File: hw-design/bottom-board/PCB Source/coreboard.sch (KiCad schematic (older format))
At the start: 21 parts, among them J5 HMI_DATA, J6 SERIAL_DEBUG, U3 AP2120N-3.3, U7 AT24CS08

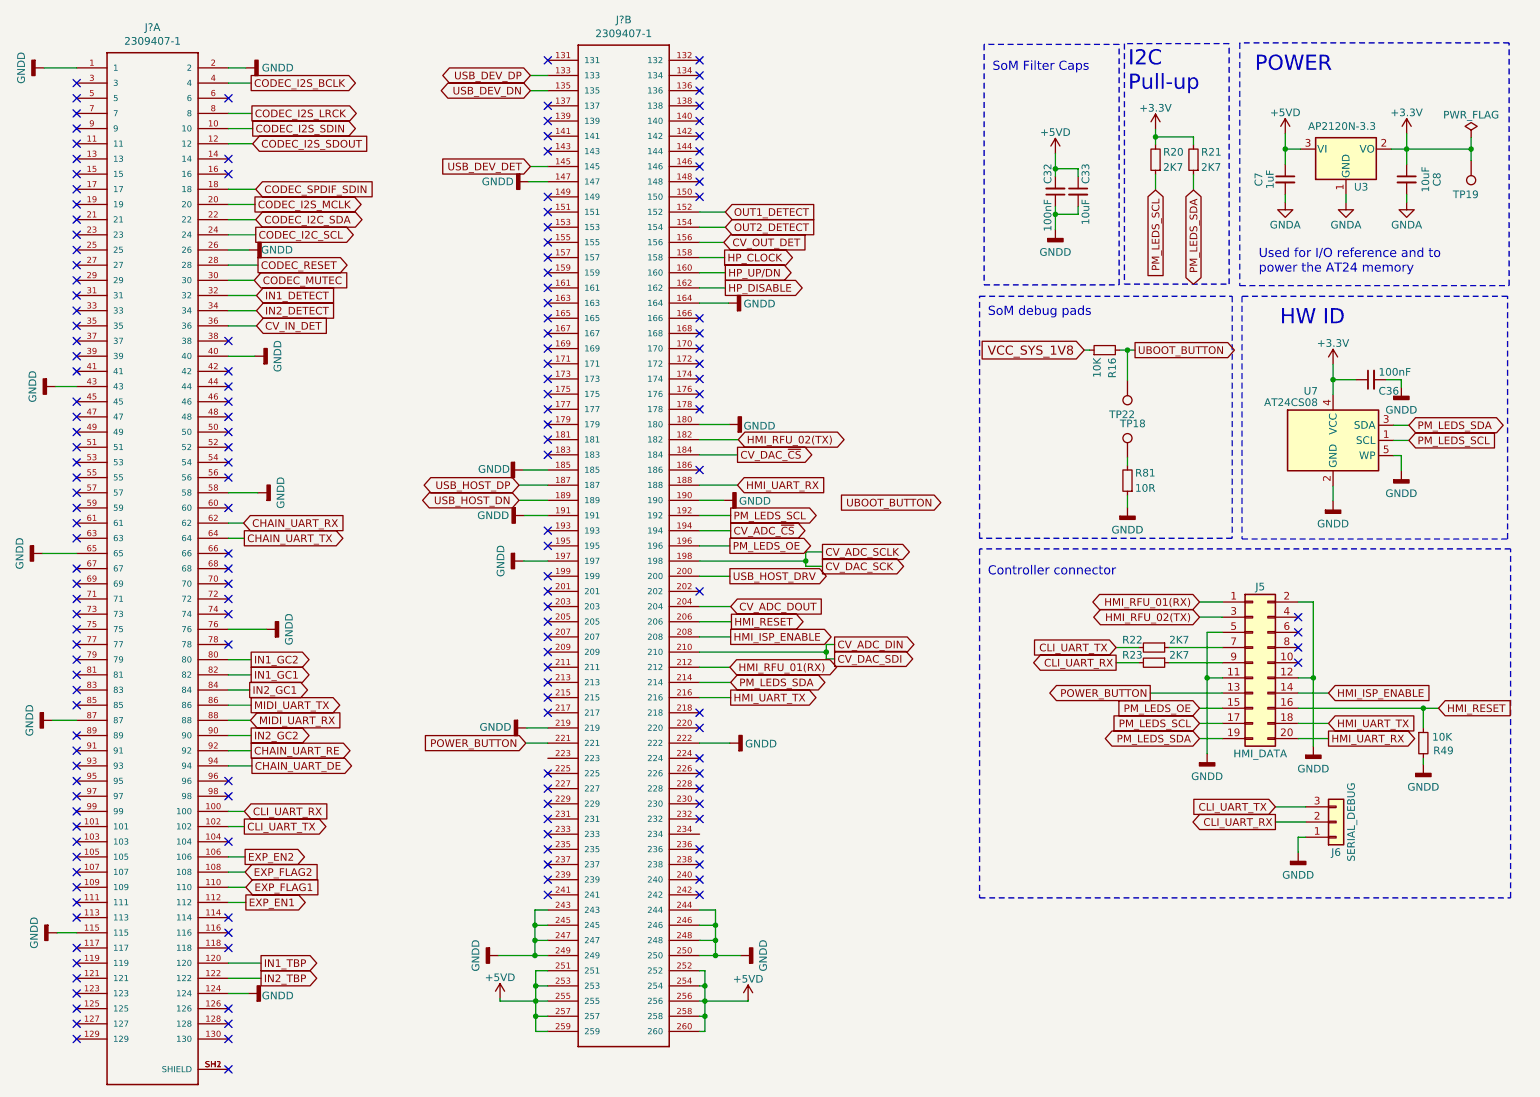
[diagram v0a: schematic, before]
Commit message: place new power curcuit on the PCB
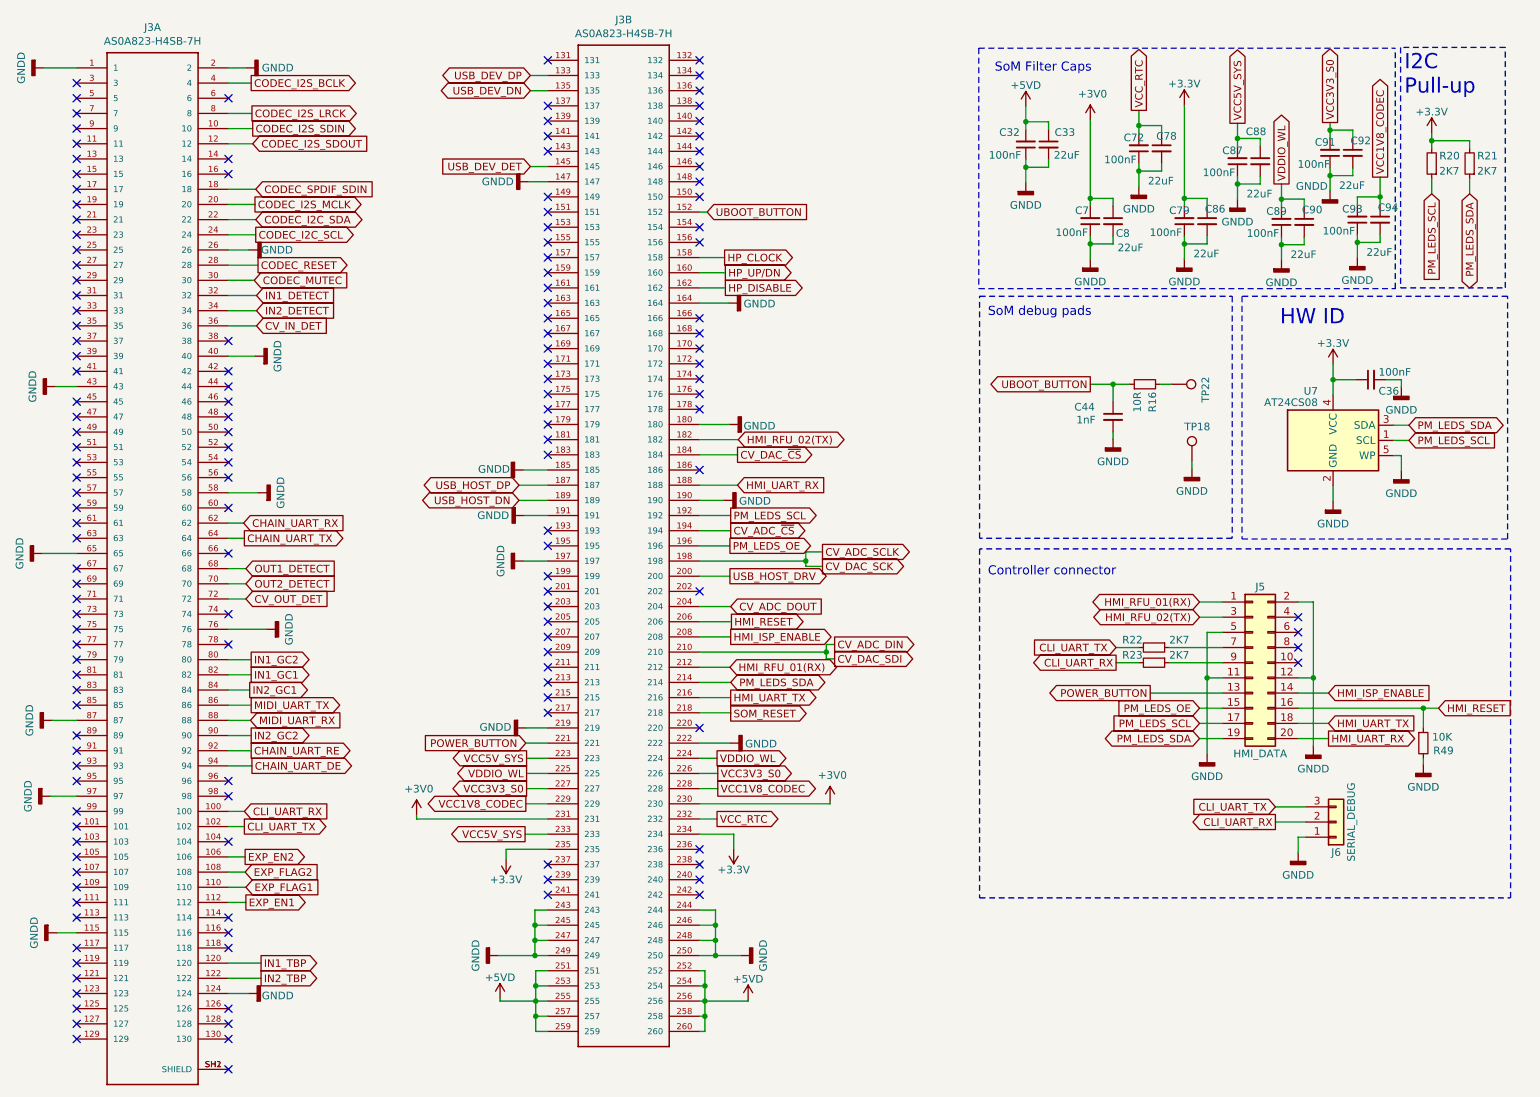
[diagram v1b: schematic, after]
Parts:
- removed R81: 10R, Resistor_SMD:R_0603_1608Metric, symbol bottom-board-rescue:R_Small-Device
- removed TP19: TestPoint, TestPoint:TestPoint_Pad_D1.0mm, symbol bottom-board-rescue:TestPoint-Connector
- removed U3: AP2120N-3.3, Package_TO_SOT_SMD:SOT-23, symbol bottom-board-rescue:AP2120N-3.3-local-components
- added C44: 1nF, Capacitor_SMD:C_0603_1608Metric, symbol bottom-board-rescue:C_Small-Device
- added C72, C79, C87, C89, C91, C93: 100nF, Capacitor_SMD:C_0603_1608Metric, symbol bottom-board-rescue:C_Small-Device
- added C78, C86, C88, C90, C92, C94: 22uF, Capacitor_SMD:C_0805_2012Metric, symbol bottom-board-rescue:C_Small-Device
- C33, C8: value 10uF -> 22uF; footprint Capacitor_SMD:C_0603_1608Metric -> Capacitor_SMD:C_0805_2012Metric; MPN CL10A106MQ8NNNC -> CL21A226MPQNNNE
- C7: value 1uF -> 100nF; MPN CL10B105KP8NNNC -> GCM188R71C104KA37D
- J3: renamed from J?; value 2309407-1 -> AS0A823-H4SB-7H; footprint TE_2309407-1 -> Uno:TE_2309409-1; Field10 TE Connectivity -> (none); Field11 DDR4 SODIMM Socket 260 Contacts 0.5mm Pitch Black Surface M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 -> (none); Field12 260 -> (none); Field13 .5 mm[.0197 in] -> (none); Field14 Socket -> (none); Field4 None -> (none); Field5 2309407-1 -> (none); Field6 None -> (none); Field7 https://www.te.com/usa-en/product-2309407-1.html?te_bu=Cor&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 -> (none); Field8 Unavailable -> (none); Field9 Compliant -> (none); MPN (none) -> AS0A823-H4SB-7H
- R16: value 10K -> 10R; MPN RR0816P-103-D -> (none)
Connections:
- net VCC_SYS_1V8 is gone; now on net UBOOT_BUTTON: R16.1
- net +3V3: now also J3.234, J3.235, C79.2, C86.1; no longer C8.1
- net +5VD: no longer C7.1
- net CV_OUT_DET: now also J3.72; no longer J3.156
- net GNDD: now also C7.1, C8.2, J3.97, TP18.1, C44.2, C72.1, C78.2, C79.1, C86.2, C87.1, C88.2, C89.1, C90.2, C91.1, C92.2, C93.1, C94.2
- net OUT1_DETECT: now also J3.68; no longer J3.152
- net OUT2_DETECT: now also J3.70; no longer J3.154
- net UBOOT_BUTTON: now also J3.152, C44.1; no longer R16.2, TP22.1
- net SOM_RESET: now reaches J3.218
- net VCC5V_SYS: now reaches J3.223
- net VCC5V_SYS: now also J3.233, C87.2, C88.1
- net VDDIO_WL: now reaches J3.224
- net VDDIO_WL: now also J3.225, C89.2, C90.1
- net VCC3V3_S0: now reaches J3.226
- net VCC3V3_S0: now also J3.227, C91.2, C92.1
- net VCC1V8_CODEC: now reaches J3.228
- net VCC1V8_CODEC: now also J3.229, C93.2, C94.1
- net +3V0: now reaches J3.230
- net +3V0: now also C7.2, C8.1, J3.231
- net VCC_RTC: now reaches J3.232
- net VCC_RTC: now also C72.2, C78.1
- removed net GNDA: C7.2, C8.2
- new net: R16.2, TP22.1
- no-connect marks 167 -> 153
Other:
- note removed: "POWER"
- note removed: "Used for I/O reference and to\npower the AT24 memory"
- moved on the sheet: C32, C33, R16, R20, R21, TP18, TP22

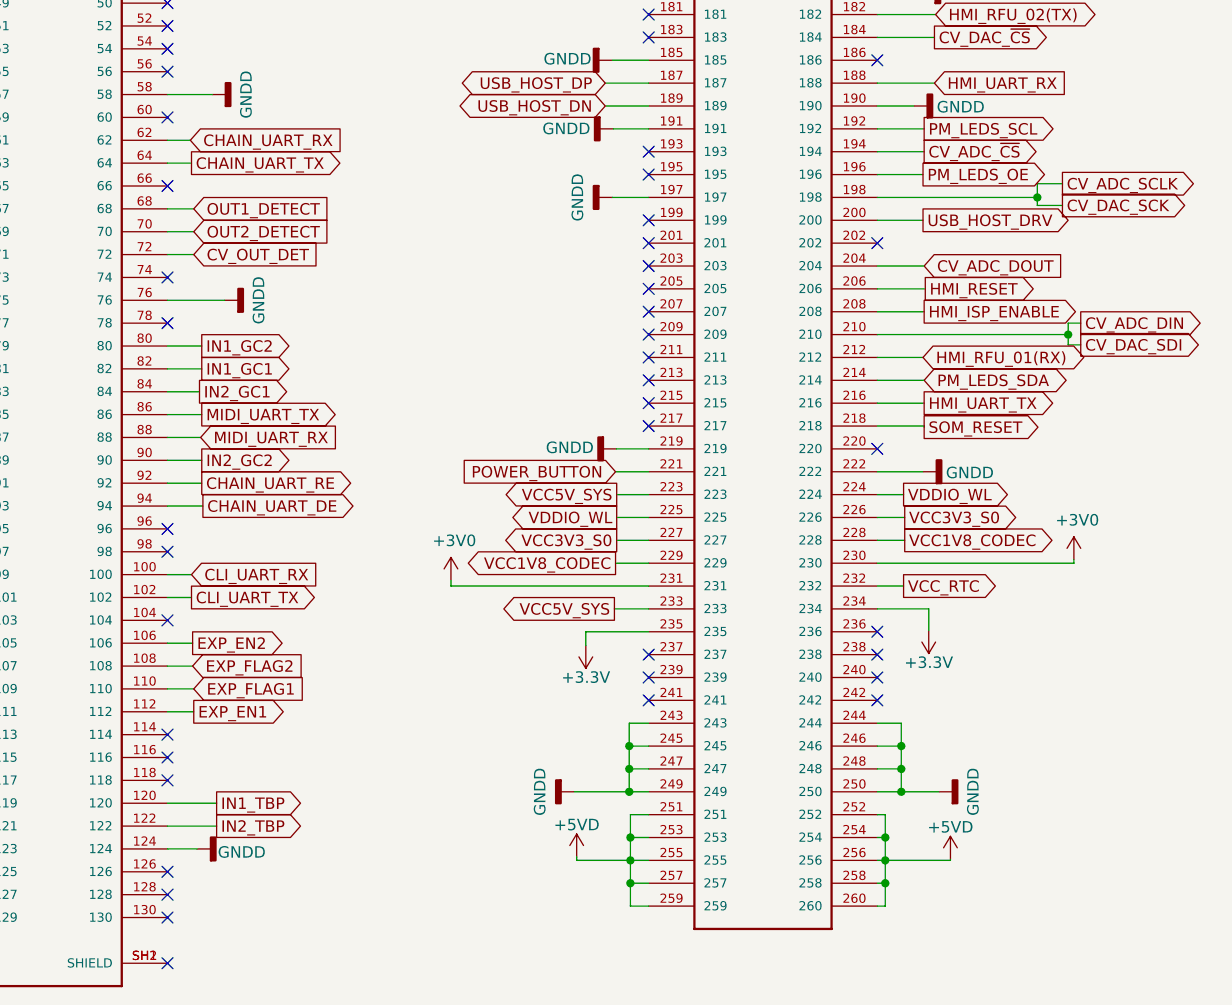
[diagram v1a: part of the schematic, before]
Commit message: route codec to new SoM
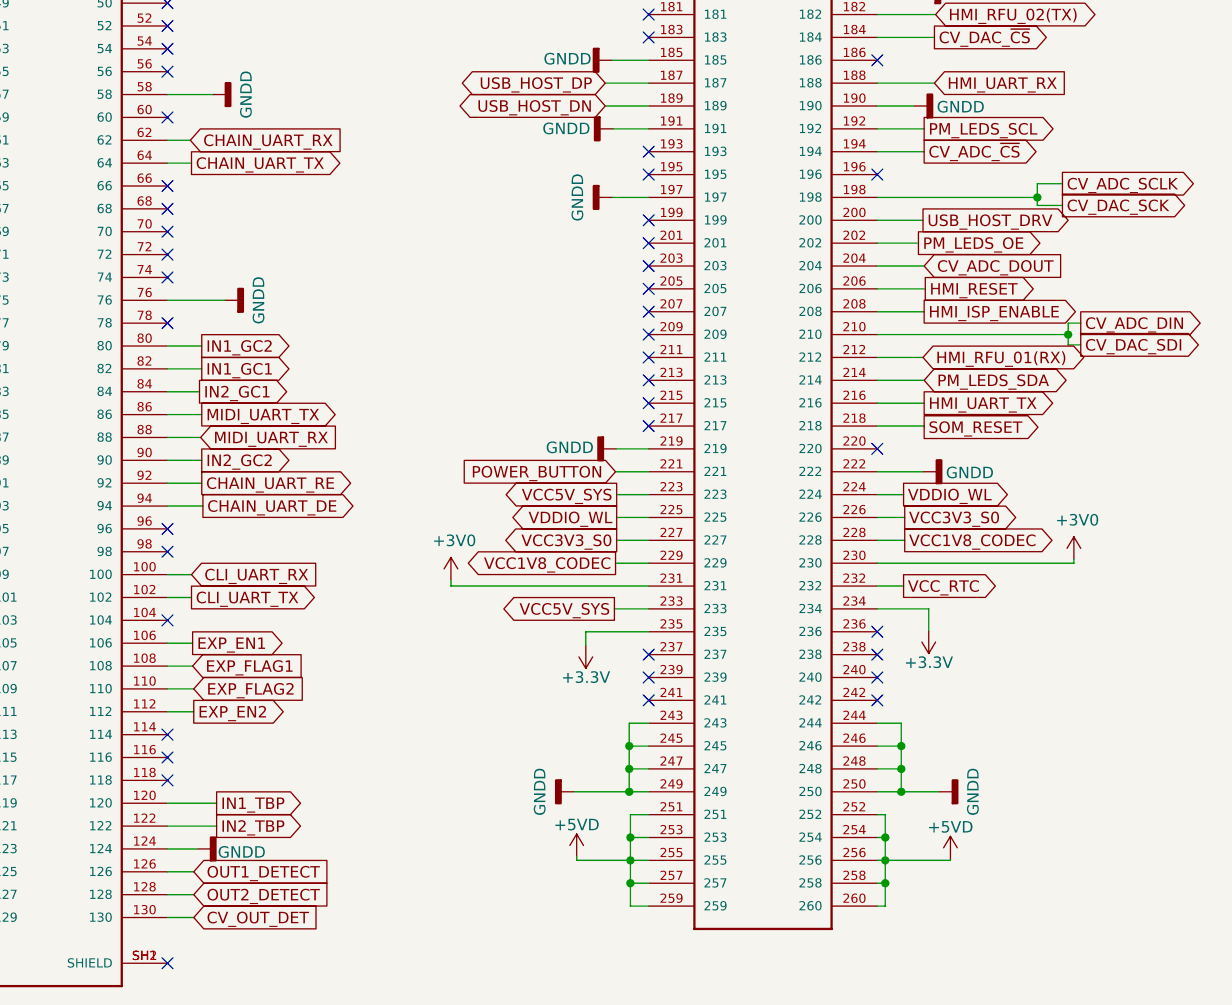
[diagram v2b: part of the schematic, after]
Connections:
- net CV_OUT_DET: now also J3.130; no longer J3.72
- net EXP_EN1: now also J3.106; no longer J3.112
- net EXP_EN2: now also J3.112; no longer J3.106
- net EXP_FLAG1: now also J3.108; no longer J3.110
- net EXP_FLAG2: now also J3.110; no longer J3.108
- net OUT1_DETECT: now also J3.126; no longer J3.68
- net OUT2_DETECT: now also J3.128; no longer J3.70
- net PM_LEDS_OE: now also J3.202; no longer J3.196
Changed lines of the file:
@@
 Text GLabel 2835 2690 2    50   Input ~ 0
 CV_IN_DET
-Text GLabel 2765 4490 2    50   Input ~ 0
+Text GLabel 2765 7390 2    50   Input ~ 0
 CV_OUT_DET
 Text GLabel 4640 1040 0    50   BiDi ~ 0
@@
 Text GLabel 5960 3940 2    50   Output ~ 0
 PM_LEDS_SCL
-Text GLabel 5955 4140 2    50   Output ~ 0
+Text GLabel 5935 4440 2    50   Output ~ 0
 PM_LEDS_OE
 Text GLabel 6005 3740 2    50   Input ~ 0
@@
 Text GLabel 5965 4640 2    50   Output ~ 0
 HMI_RESET
+Text GLabel 2765 6390 2    50   Input ~ 0
+EXP_FLAG2
 Text GLabel 2760 6290 2    50   Input ~ 0
-EXP_FLAG2
-Text GLabel 2765 6390 2    50   Input ~ 0
 EXP_FLAG1
+Text GLabel 2760 6190 2    50   Output ~ 0
+EXP_EN1
 Text GLabel 2765 6490 2    50   Output ~ 0
-EXP_EN1
-Text GLabel 2760 6190 2    50   Output ~ 0
 EXP_EN2
 Text GLabel 2845 2290 2    50   Output ~ 0
@@
 Text GLabel 2835 2590 2    50   Input ~ 0
 IN2_DETECT
-Text GLabel 2765 4290 2    50   Input ~ 0
+Text GLabel 2765 7190 2    50   Input ~ 0
 OUT1_DETECT
-Text GLabel 2765 4390 2    50   Input ~ 0
+Text GLabel 2765 7290 2    50   Input ~ 0
 OUT2_DETECT
 $Comp
@@
 Wire Wire Line
 	5755 4040 5960 4040
-Wire Wire Line
-	5755 4140 5955 4140
 Wire Wire Line
 	5755 4340 5955 4340
@@
 NoConn ~ 1650 7290
 NoConn ~ 1650 7390
-NoConn ~ 2650 7390
-NoConn ~ 2650 7290
-NoConn ~ 2650 7190
 NoConn ~ 2650 6790
 NoConn ~ 2650 6690
@@
 NoConn ~ 4755 5240
 NoConn ~ 5755 5340
-NoConn ~ 5755 4440
 NoConn ~ 5755 3640
 NoConn ~ 5755 3240
@@
 	1650 5790 1480 5790
 Wire Wire Line
-	2650 4290 2765 4290
-Wire Wire Line
-	2650 4390 2765 4390
-Wire Wire Line
-	2650 4490 2765 4490
+	2650 7190 2765 7190
+Wire Wire Line
+	2650 7290 2765 7290
+Wire Wire Line
+	2650 7390 2765 7390
 $Comp
 L bottom-board-rescue:C_Small-Device C44
@@
 Wire Wire Line
 	3890 5940 4755 5940
+NoConn ~ 2650 4290
+NoConn ~ 2650 4390
+NoConn ~ 2650 4490
+Wire Wire Line
+	5755 4440 5935 4440
+NoConn ~ 5755 4140
 $EndSCHEMATC

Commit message: update all MPN's to match the Dwarf
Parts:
- J3: MPN AS0A823-H4SB-7H -> TE_2309409-1
- J5: MPN 302-S201 -> SBH11-PBPC-D10-ST-BK
- R16: MPN (none) -> CRGCQ0603J10R
- R20, R21, R22, R23: MPN RMCF0603JT2K70 -> CRGCQ0603F2K7
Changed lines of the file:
@@
 Sheet 4 13
 Title "MOD DuoX - Bottom Board"
-Date "2020-05-15"
-Rev "Rev 1.12"
+Date "2021-11-11"
+Rev "Rev 1.05"
 Comp "MOD Devices GmbH"
 Comment1 "DuoX Audio processing board"
 Comment2 "https://github.com/moddevices/mod-hw-duoX"
-Comment3 ""
-Comment4 ""
+Comment3 "Inp Power: 12V 700mA"
+Comment4 "USB outp Power: 500mA"
 $EndDescr
 $Comp
@@
 F 2 "Resistor_SMD:R_0603_1608Metric" H 10580 1620 60  0001 C CNN
 F 3 "" H 10580 1620 60  0000 C CNN
-F 4 "RMCF0603JT2K70" H 2130 -230 50  0001 C CNN "MPN"
+F 4 "CRGCQ0603F2K7" H 2130 -230 50  0001 C CNN "MPN"
 	1    10580 1620
 	-1   0    0    1
@@
 F 2 "footprints:Pin_Header_Straight_2x10_Shrouded" H 9400 4910 50  0001 C CNN
 F 3 "" H 9400 4910 50  0001 C CNN
-F 4 "302-S201" H 9400 4910 50  0001 C CNN "MPN"
+F 4 "SBH11-PBPC-D10-ST-BK" H 9400 4910 50  0001 C CNN "MPN"
 	1    9400 4910
 	1    0    0    -1
@@
 F 2 "Resistor_SMD:R_0603_1608Metric" H 10830 1620 60  0001 C CNN
 F 3 "" H 10830 1620 60  0000 C CNN
-F 4 "RMCF0603JT2K70" H 2380 -230 50  0001 C CNN "MPN"
+F 4 "CRGCQ0603F2K7" H 2380 -230 50  0001 C CNN "MPN"
 	1    10830 1620
 	-1   0    0    1
@@
 F 2 "Resistor_SMD:R_0603_1608Metric" H 8750 4810 60  0001 C CNN
 F 3 "" H 8750 4810 60  0000 C CNN
-F 4 "RMCF0603JT2K70" H 300 2960 50  0001 C CNN "MPN"
+F 4 "CRGCQ0603F2K7" H 300 2960 50  0001 C CNN "MPN"
 	1    8750 4810
 	0    1    1    0
@@
 F 2 "Resistor_SMD:R_0603_1608Metric" H 8750 4910 60  0001 C CNN
 F 3 "" H 8750 4910 60  0000 C CNN
-F 4 "RMCF0603JT2K70" H 300 3060 50  0001 C CNN "MPN"
+F 4 "CRGCQ0603F2K7" H 300 3060 50  0001 C CNN "MPN"
 	1    8750 4910
 	0    1    1    0
@@
 F 2 "Resistor_SMD:R_0603_1608Metric" H 8690 3075 60  0001 C CNN
 F 3 "" H 8690 3075 60  0000 C CNN
+F 4 "CRGCQ0603J10R" H 8690 3075 50  0001 C CNN "MPN"
 	1    8690 3075
 	0    -1   -1   0
@@
 F 2 "Uno:TE_2309409-1" H 5255 4140 50  0001 L BNN
 F 3 "2309407-1" H 5255 4140 50  0001 L BNN
-F 4 "AS0A823-H4SB-7H" H 5255 4140 50  0001 L BNN "MPN"
+F 4 "TE_2309409-1" H 5255 4140 50  0001 L BNN "MPN"
 	2    5255 4140
 	1    0    0    -1

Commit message: update fabrication files
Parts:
- TP18, TP22: footprint TestPoint:TestPoint_Pad_D1.0mm -> TestPoint:TestPoint_Loop_D1.80mm_Drill1.0mm_Beaded
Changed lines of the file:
@@
 F 0 "TP18" H 8950 3805 50  0000 L CNN
 F 1 "TestPoint" H 9058 3609 50  0001 L CNN
-F 2 "TestPoint:TestPoint_Pad_D1.0mm" H 9200 3580 50  0001 C CNN
+F 2 "TestPoint:TestPoint_Loop_D1.80mm_Drill1.0mm_Beaded" H 9200 3580 50  0001 C CNN
 F 3 "~" H 9200 3580 50  0001 C CNN
 	1    9000 3580
@@
 F 0 "TP22" H 8815 3300 50  0000 L CNN
 F 1 "TestPoint" H 8923 3104 50  0001 L CNN
-F 2 "TestPoint:TestPoint_Pad_D1.0mm" H 9065 3075 50  0001 C CNN
+F 2 "TestPoint:TestPoint_Loop_D1.80mm_Drill1.0mm_Beaded" H 9065 3075 50  0001 C CNN
 F 3 "~" H 9065 3075 50  0001 C CNN
 	1    8865 3075

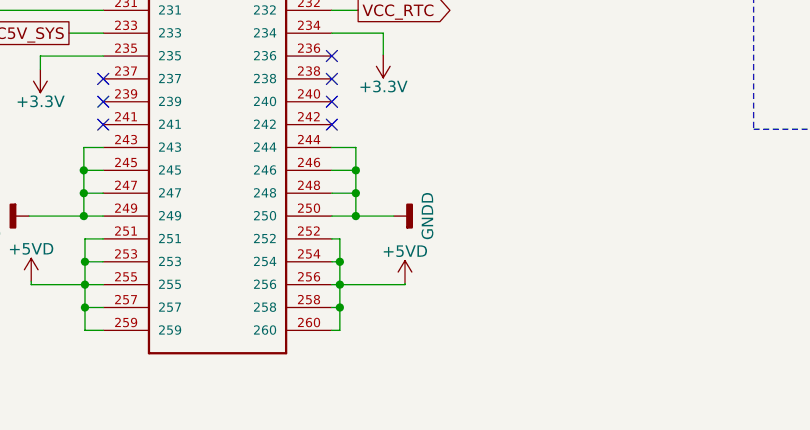
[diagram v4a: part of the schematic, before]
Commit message: fix U1 ()10V regulator footprint
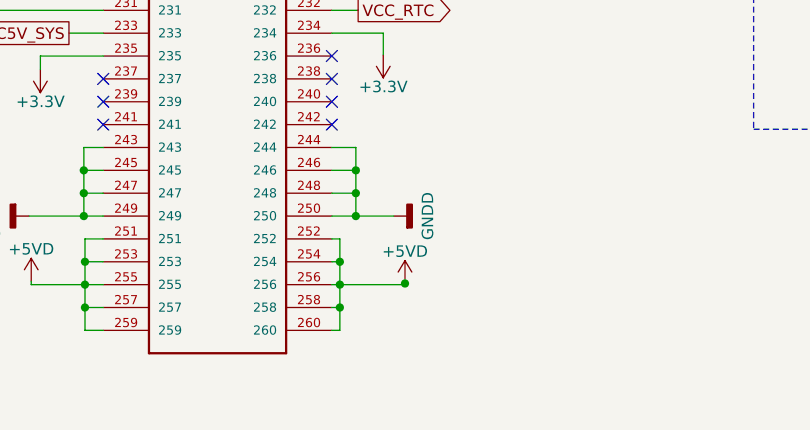
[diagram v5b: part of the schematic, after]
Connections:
- net CV_ADC_~CS~ renamed CV_ADC_~{CS}
- net CV_DAC_~CS~ renamed CV_DAC_~{CS}
